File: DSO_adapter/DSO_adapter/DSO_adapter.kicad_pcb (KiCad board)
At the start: 2 copper layers, 71 x 15 mm, 12 parts, among them J1 Conn_02x05_Odd_Even, J2 AudioJack2_SwitchT, J3 AudioJack2_SwitchT, J4 Conn_01x02_Male, J5 Conn_01x02_Male, U1 LM7805_TO220

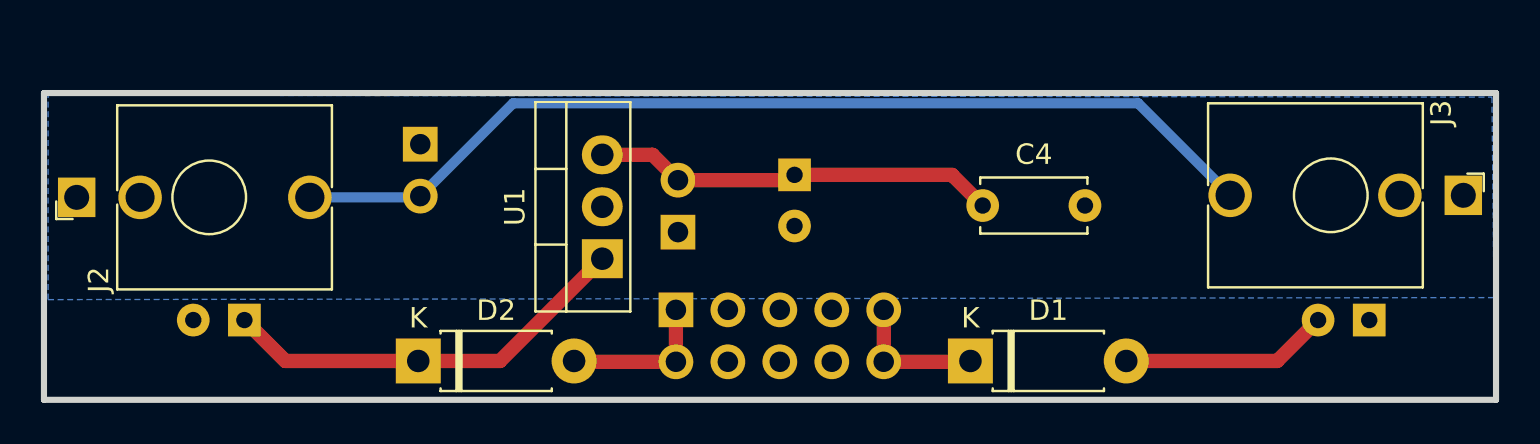
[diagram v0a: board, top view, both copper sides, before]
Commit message: Corrections made to ground planes, trace widths, etc. after visual checks of printout
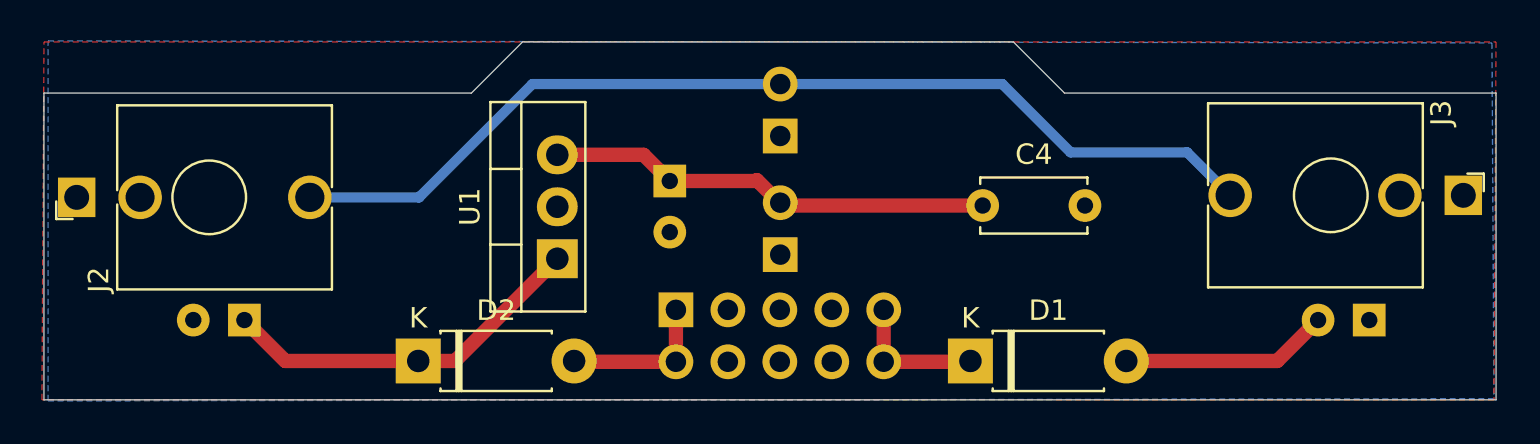
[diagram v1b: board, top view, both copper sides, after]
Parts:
- moved J4 17.6 mm to (56.1, 24.1), turned to 0 degrees
- moved C3 6.11 mm to (50.7, 26.3)
- moved J5 5.12 mm to (56.1, 29.9)
- moved U1 2.20 mm to (45.2, 30.1)
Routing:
- net Net-(C2-Pad1): track 20.4 -> 18.2 mm
- net Net-(C3-Pad1): track 19.8 -> 21.9 mm
- net Net-(J2-PadT): track 48.8 -> 49.6 mm
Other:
- board size 71 x 15 mm -> 71 x 17.5 mm
